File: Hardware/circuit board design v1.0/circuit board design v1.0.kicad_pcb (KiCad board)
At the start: 4 copper layers, 30 x 74 mm, 48 parts, among them IC1 BMI088, J1 Conn_01x06_Male, J2 Conn_01x02, J3 105017-0001, J4 Conn_01x04, Q1 2N7002-7-F, U1 STM32F446RETx, U2 W25Q64JVSS, U3 SDR08540M3-01, U4 BME280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

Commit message: Redid footprint for buzzer
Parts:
- added C22: 1uF, Capacitor_SMD:C_0603_1608Metric_Pad1.08x0.95mm_HandSolder, B.Cu at (33.4, 77.6)
- added C23: 1uF, Capacitor_SMD:C_0603_1608Metric_Pad1.08x0.95mm_HandSolder, B.Cu at (35.8, 77.6)
- added C24: 1uF, Capacitor_SMD:C_0603_1608Metric_Pad1.08x0.95mm_HandSolder, B.Cu at (31.2, 74.8)
- C10, C11, C12, C13, C7, C8: value 100n -> 100nF
- C21: footprint Capacitor_THT:CP_Radial_D5.0mm_P2.00mm -> Capacitor_SMD:C_0603_1608Metric
- D2: value D_Schottky -> DFLS130L
- U7: value NCP161ASN180T1G -> NCP161ASN330T1G
- U8: value L80-R -> L80-M39
- moved C21 26.6 mm to (24.0, 46.4), turned to 0 degrees
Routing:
- net +3.3V: track 53.8 -> 61.6 mm, vias 17 -> 21
- net GND: track 79.7 -> 86.1 mm, vias 35 -> 78
- net Net-(R5-Pad1): track 22.7 -> 18.3 mm
- net +3.3VA: track 41.2 -> 40.7 mm
- added copper zone on B.Cu, net GND
- added copper zone on F.Cu, net GND
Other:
- board text added: "IC SpaceSoc Flight Computer V2.0 2023"
- board text added: "JLCJLCJLCJLC"
- board text removed: "IC SpaceSoc Flight Computer V1.0 2023"

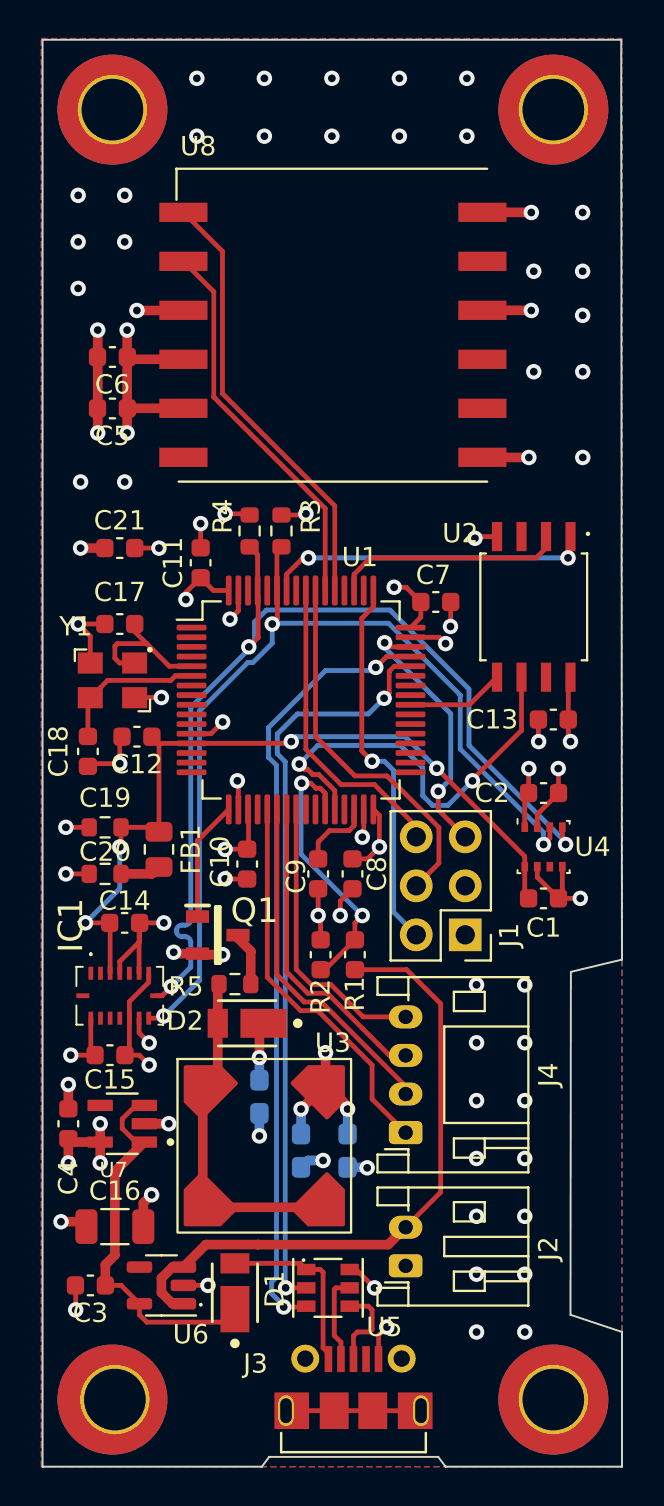
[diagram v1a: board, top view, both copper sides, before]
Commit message: Added radio connections to pcb and code
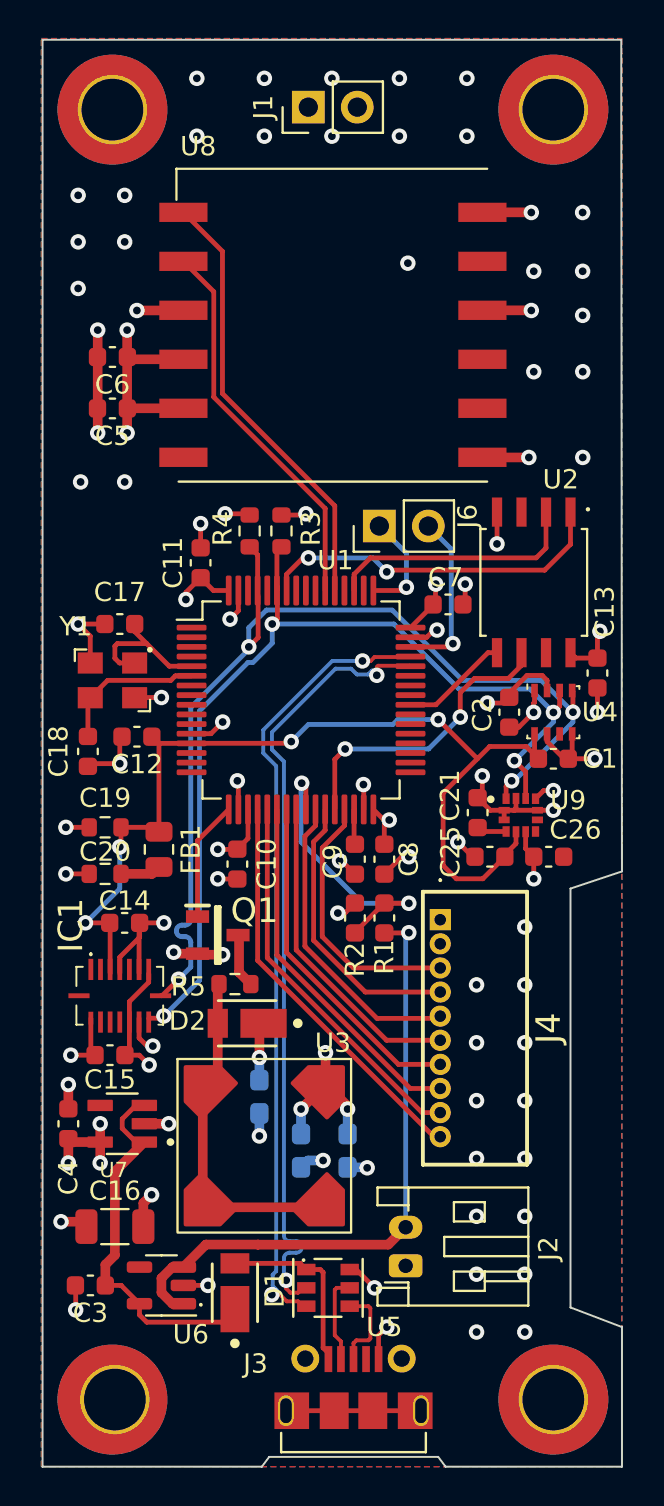
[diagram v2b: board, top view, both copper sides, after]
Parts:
- added C25: 100nF, Capacitor_SMD:C_0603_1608Metric, F.Cu at (43.2, 62.4)
- added C26: 100nF, Capacitor_SMD:C_0603_1608Metric, F.Cu at (46.2, 62.4)
- added J6: Conn_01x02_Male, Connector_PinHeader_2.54mm:PinHeader_1x02_P2.54mm_Vertical, F.Cu at (37.5, 45.2)
- added U9: LIS3MDLTR, Components:XDCR_LIS3MDLTR, F.Cu at (44.8, 60.2)
- C16: value 1uF -> 4.7uF
- C21: value 4.7uF -> 100nF
- J1: value Conn_01x06_Male -> Conn_01x02_Male; footprint Connector_PinHeader_2.54mm:PinHeader_2x03_P2.54mm_Vertical -> Connector_PinHeader_2.54mm:PinHeader_1x02_P2.54mm_Vertical
- J4: value Conn_01x04 -> DF13-10P-1.25DS_20_; footprint Components:JST_PH_S4B-PH-K_1x04_P2.00mm_Horizontal -> Components:DF1310P125DS20
- moved J1 43.7 mm to (33.8, 23.5), turned to 90 degrees
- moved C21 23.1 mm to (42.6, 60.1), turned to 90 degrees
- moved J4 11.2 mm to (40.6, 65.6), turned to -90 degrees
- moved C1 7.26 mm to (46.5, 57.3)
- moved U4 7.00 mm to (46.5, 54.9)
- moved C2 4.55 mm to (44.2, 54.9), turned to -90 degrees
- moved C13 3.32 mm to (48.8, 52.8), turned to -90 degrees
- moved R2 2.61 mm to (36.2, 65.5)
- moved R1 2.44 mm to (37.7, 65.5)
- moved C9 2.05 mm to (36.2, 62.5)
- moved C8 1.82 mm to (37.7, 62.5)
- moved U2 1.27 mm to (45.5, 48.1)
- moved C7 0.65 mm to (41.0, 49.3)
- moved C10 0.51 mm to (30.1, 62.7)
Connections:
- net /MCU/usb_dm renamed /MCU/usb_d-
- net /MCU/usb_dp renamed /MCU/usb_d+
- net Net-(J3-Pad2) renamed /Power/D-
- net Net-(J3-Pad3) renamed /Power/D+
- C21 pad 1: +3.3V -> Net-(C21-Pad1)
- J1 pad 2: /MCU/SYS_JTCK_SWCLK -> GND
- J4 pad 1: /MCU/SPI1_SCK -> +3.3V
- J4 pad 2: /MCU/SPI1_MISO -> GND
- J4 pad 3: /MCU/SPI1_MOSI -> /MCU/Radio_TX
- J4 pad 4: /MCU/Radio_Enable -> /MCU/Radio_RX
- U1 pad 20: unconnected-(U1-Pad20) -> /MCU/Radio_DIO0
- U1 pad 25: unconnected-(U1-Pad25) -> /MCU/PWR_BVOLTS
- U1 pad 26: unconnected-(U1-Pad26) -> /MCU/Radio_DIO1
- U1 pad 27: /MCU/PWR_BVOLTS -> /MCU/Radio_RX
- U1 pad 29: unconnected-(U1-Pad29) -> /MCU/Radio_TX
- U1 pad 50: /MCU/SYS_JTDI -> unconnected-(U1-Pad50)
- U1 pad 55: /MCU/SYS_JTRST -> unconnected-(U1-Pad55)
- U1 pad 56: /MCU/SYS_JTDO_SWO -> unconnected-(U1-Pad56)
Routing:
- net /MCU/Radio_DIO0: track 0.00 -> 20.9 mm
- net /MCU/SYS_JTRST: track 19.4 -> 0.00 mm
- net /MCU/SYS_JTDO_SWO: track 16.5 -> 0.00 mm
- net /MCU/Radio_DIO1: track 0.00 -> 15.8 mm
- net /MCU/Radio_RX: track 0.00 -> 14.6 mm
- net /MCU/SYS_JTCK_SWCLK: track 19.6 -> 5.54 mm
- net /MCU/Radio_TX: track 0.00 -> 13.7 mm
- net +3.3VA: track 40.7 -> 51.3 mm
- net /MCU/QUADSPI_CLK: track 21.9 -> 15.7 mm
- net GND: track 86.1 -> 91.7 mm, vias 78 -> 83
- net /MCU/SYS_JTMS_SWDIO: track 13.8 -> 8.89 mm, vias 2 -> 1
- net Net-(C9-Pad1): track 3.93 -> 1.82 mm
- net /MCU/usb_d-: track 39.0 -> 41.0 mm
- net /MCU/SCL: track 52.0 -> 53.9 mm, vias 3 -> 4
- net /MCU/Radio_Enable: track 15.0 -> 16.6 mm
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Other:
- outline, holes or cut-outs redrawn

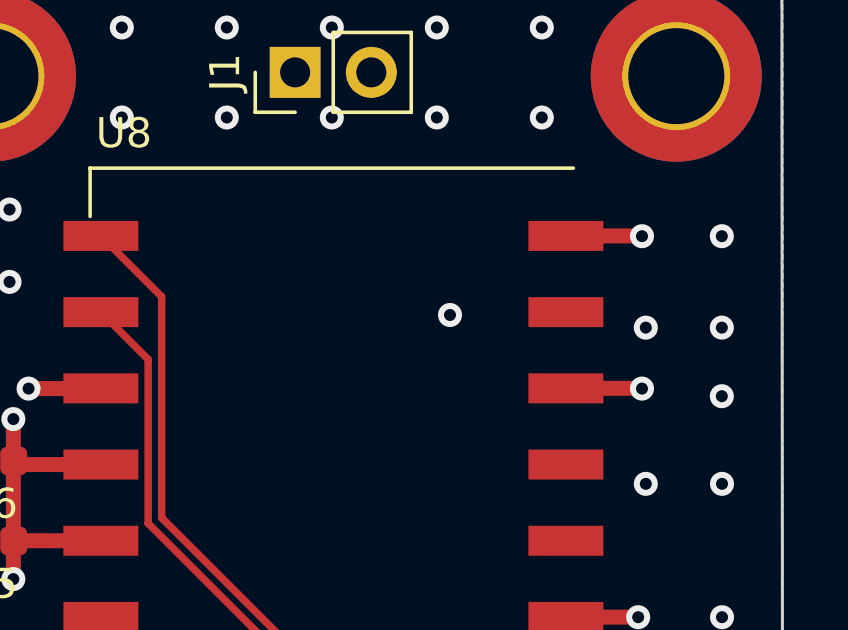
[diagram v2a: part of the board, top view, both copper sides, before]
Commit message: Design before mounting radio on surface
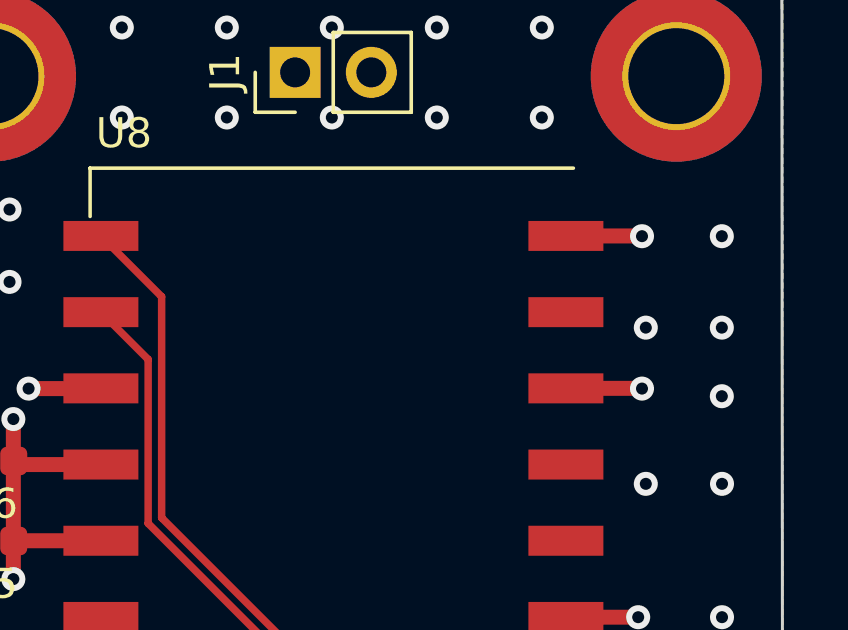
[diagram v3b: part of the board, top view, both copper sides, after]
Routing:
- net GND: vias 83 -> 82
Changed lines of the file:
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@@
   (via (at 26.543 76.2) (size 0.8) (drill 0.4) (layers "F.Cu" "B.Cu") (free) (net 47))
   (via (at 21.844 30.48) (size 0.8) (drill 0.4) (layers "F.Cu" "B.Cu") (free) (net 47))
-  (via (at 38.939 31.583) (size 0.8) (drill 0.4) (layers "F.Cu" "B.Cu") (free) (net 47))
   (segment (start 34.544 78.105) (end 33.7555 78.105) (width 0.5) (layer "B.Cu") (net 47))
   (segment (start 36.8035 78.4595) (end 36.83 78.486) (width 0.25) (layer "B.Cu") (net 47))

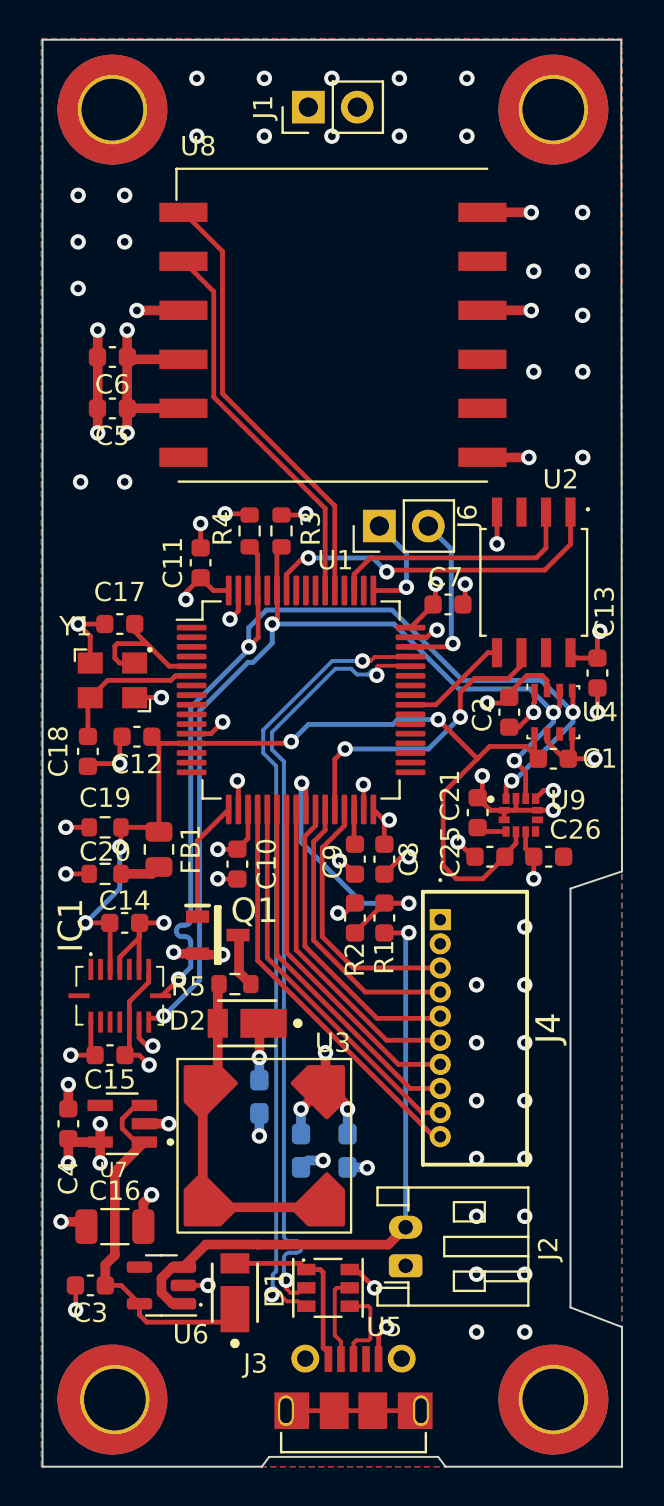
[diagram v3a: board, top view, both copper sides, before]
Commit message: Added routing for radio module on back of pcb
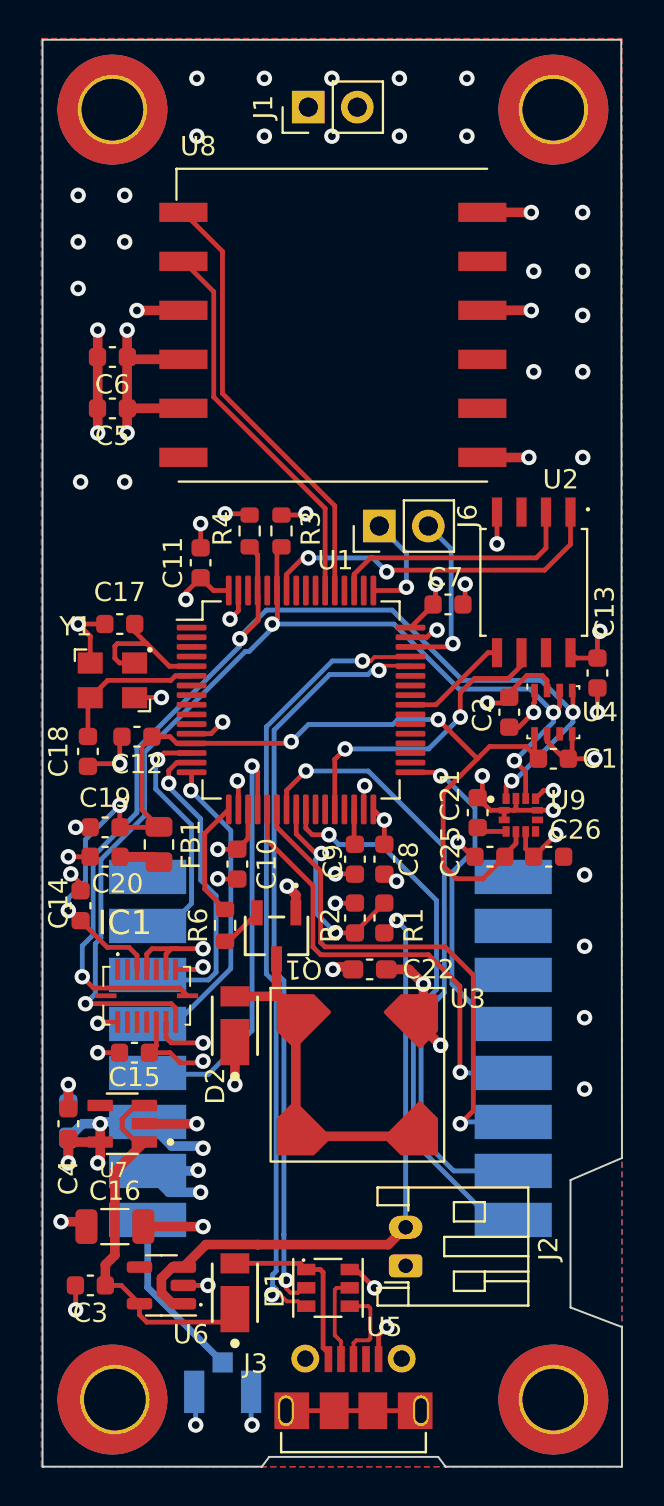
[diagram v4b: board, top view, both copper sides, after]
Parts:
- removed C23, C24: 1uF, Capacitor_SMD:C_0603_1608Metric_Pad1.08x0.95mm_HandSolder
- removed R5: 68, Resistor_SMD:R_0603_1608Metric
- added C27: 100nF, Capacitor_SMD:C_0603_1608Metric_Pad1.08x0.95mm_HandSolder, B.Cu at (21.3, 76.1)
- added R6: 3.3k, Resistor_SMD:R_0603_1608Metric, F.Cu at (29.5, 65.9)
- added U10: LAMBDA-9D, Components:XCVR_LAMBDA-9D, B.Cu at (34.9, 74.0)
- C17, C18: value 8pF -> 15pF
- C19, C20: footprint Resistor_SMD:R_0603_1608Metric -> Capacitor_SMD:C_0603_1608Metric
- C22: value 1uF -> 4.7uF; moved to F.Cu
- J4: value DF13-10P-1.25DS_20_ -> U.FL-R-SMT-1_10_; footprint Components:DF1310P125DS20 -> Components:U.FL-R-SMT-1_10_; moved to B.Cu
- Q1: value 2N7002-7-F -> 2SCR512R_HZG; footprint Components:SOT96P240X120-3N -> Components:2SCR512RHZG
- Y1: value Crystal_GND24 -> ECS-80-8-33Q-ADS-TR3
- moved J4 27.0 mm to (29.3, 90.1), turned to 180 degrees
- moved C22 10.0 mm to (37.0, 68.2), turned to 180 degrees
- moved U3 6.07 mm to (36.3, 73.7)
- moved Q1 3.05 mm to (32.1, 66.5), turned to 180 degrees
- moved C14 2.45 mm to (22.0, 64.9), turned to 90 degrees
- moved IC1 1.40 mm to (25.4, 69.6)
- moved C15 1.28 mm to (24.8, 72.5)
- moved C20 0.89 mm to (23.2, 62.4)
- moved D2 0.65 mm to (30.0, 71.1), turned to -90 degrees
- moved FB1 0.25 mm to (26.0, 61.7)
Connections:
- J4 pad 1: +3.3V -> GND
- J4 pad 3: /MCU/Radio_TX -> Net-(J4-Pad3)
- Q1 pad 1: /MCU/buzzer_gate -> GND
- Q1 pad 2: GND -> Net-(Q1-Pad2)
- Q1 pad 3: Net-(Q1-Pad3) -> Net-(D2-Pad2)
- U1 pad 14: unconnected-(U1-Pad14) -> /MCU/Radio_DIO1
- U1 pad 15: unconnected-(U1-Pad15) -> /MCU/Radio_DIO0
- U1 pad 16: unconnected-(U1-Pad16) -> /MCU/Radio_RX
- U1 pad 20: /MCU/Radio_DIO0 -> /MCU/Radio_TX
- U1 pad 24: /MCU/Radio_Enable -> /MCU/PWR_BVOLTS
- U1 pad 25: /MCU/PWR_BVOLTS -> /MCU/Radio_Enable
- U1 pad 26: /MCU/Radio_DIO1 -> unconnected-(U1-Pad26)
- U1 pad 27: /MCU/Radio_RX -> unconnected-(U1-Pad27)
- U1 pad 29: /MCU/Radio_TX -> unconnected-(U1-Pad29)
- U1 pad 33: unconnected-(U1-Pad33) -> /MCU/Radio_Reset
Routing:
- net /MCU/Radio_Reset: track 0.00 -> 17.8 mm, vias 0 -> 1
- net /MCU/SPI1_MOSI: track 17.6 -> 32.3 mm, vias 0 -> 1
- net /MCU/Radio_Enable: track 16.6 -> 29.2 mm, vias 0 -> 1
- net Net-(J4-Pad3): track 0.00 -> 9.00 mm
- net /MCU/Radio_TX: track 13.7 -> 22.5 mm, vias 0 -> 1
- net /MCU/SPI1_MISO: track 18.7 -> 27.2 mm, vias 0 -> 1
- net GND: track 91.7 -> 99.1 mm, vias 82 -> 74
- net +3.3V: track 62.9 -> 69.4 mm, vias 22 -> 23
- net /MCU/SDA: track 51.4 -> 57.0 mm
- net /MCU/SCL: track 53.9 -> 59.3 mm
- net /MCU/Radio_DIO0: track 20.9 -> 16.6 mm, vias 0 -> 1
- net +3.3VA: track 51.3 -> 55.3 mm
- net /MCU/PWR_BVOLTS: track 14.9 -> 10.8 mm
- net /MCU/SPI1_SCK: track 19.8 -> 23.8 mm, vias 0 -> 1
- net /MCU/Radio_DIO1: track 15.8 -> 12.9 mm, vias 0 -> 1
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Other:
- outline, holes or cut-outs redrawn

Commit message: PCB sent for production
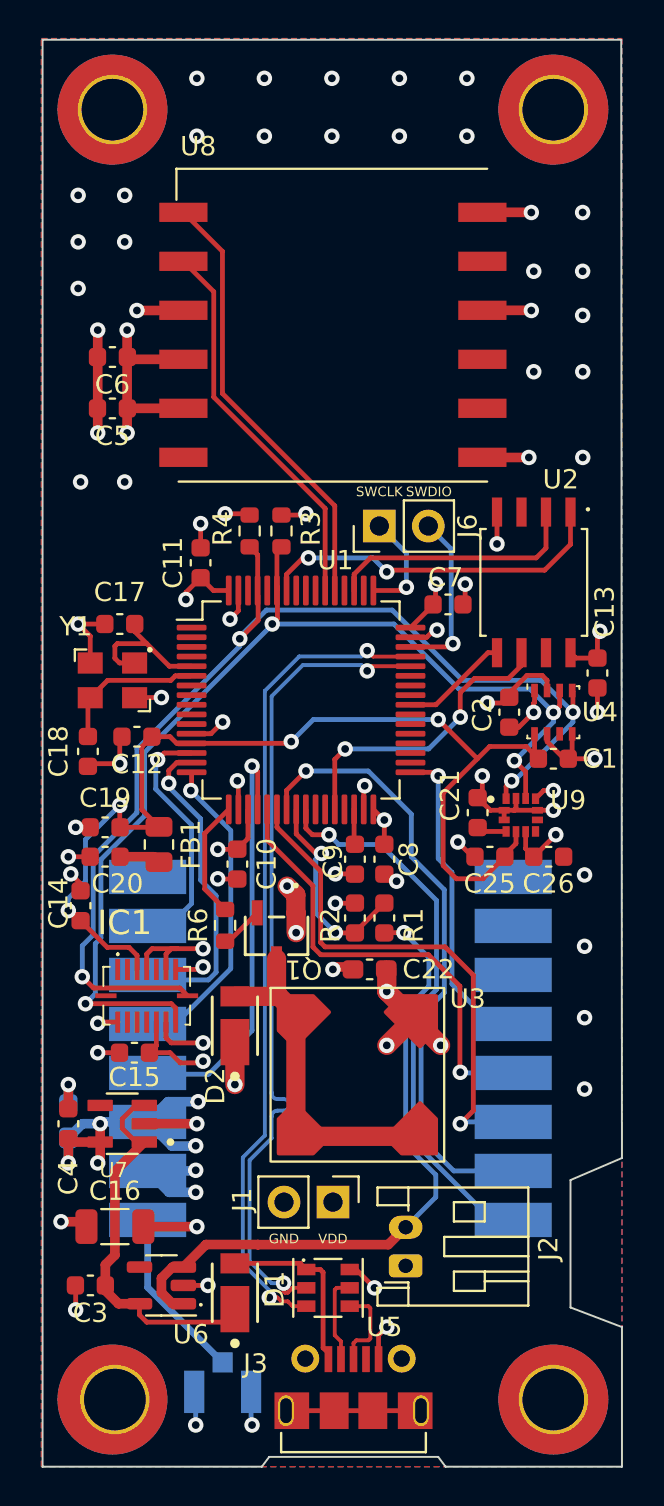
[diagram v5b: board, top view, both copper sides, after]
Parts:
- added G***: LOGO, Components:ICSS_Logo, B.Cu at (35.3, 33.8)
- moved J1 56.8 mm to (35.1, 80.3), turned to -90 degrees
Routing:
- net +3.3V: track 69.4 -> 73.7 mm, vias 23 -> 25
- net /MCU/usb_d-: track 39.0 -> 43.1 mm
- net /MCU/usb_d+: track 40.9 -> 43.1 mm
- net Net-(J2-Pad2): track 32.9 -> 34.5 mm
- net /MCU/Radio_Reset: track 17.8 -> 16.6 mm
- net GND: track 99.1 -> 99.6 mm, vias 74 -> 75
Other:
- board text added: "Flight Computer V2.0 2023"
- board text added: "Lou Alsteens Richard Hu Jakub Jędrzejewski Benny Liu Timothy Newman Václav Pavlícek"
- board text removed: "IC SpaceSoc Flight Computer V2.0 2023"
